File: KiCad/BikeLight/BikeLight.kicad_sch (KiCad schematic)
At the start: 19 parts, among them J1 Conn-01x02_P2.5mm_S2B-XH-A-BK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, J3 Conn-01x02_P2.5mm_S2B-XH-A-BK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, SW1 CK_KMS2xxG, U1 HT-CT62, U2 MPU-6050, U3 MCP1826S-33, U4 MAX17048, U5 TP4056-42-ESOP8, U6 MT3608

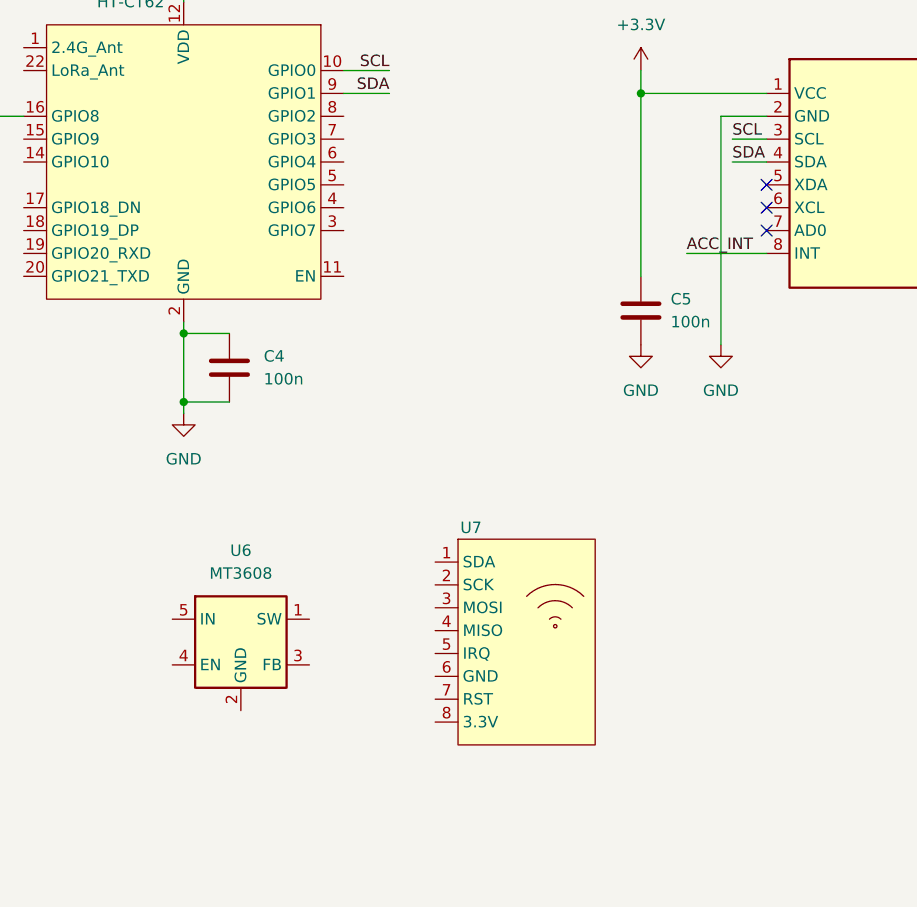
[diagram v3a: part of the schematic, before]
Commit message: Small adjustments to the RFID
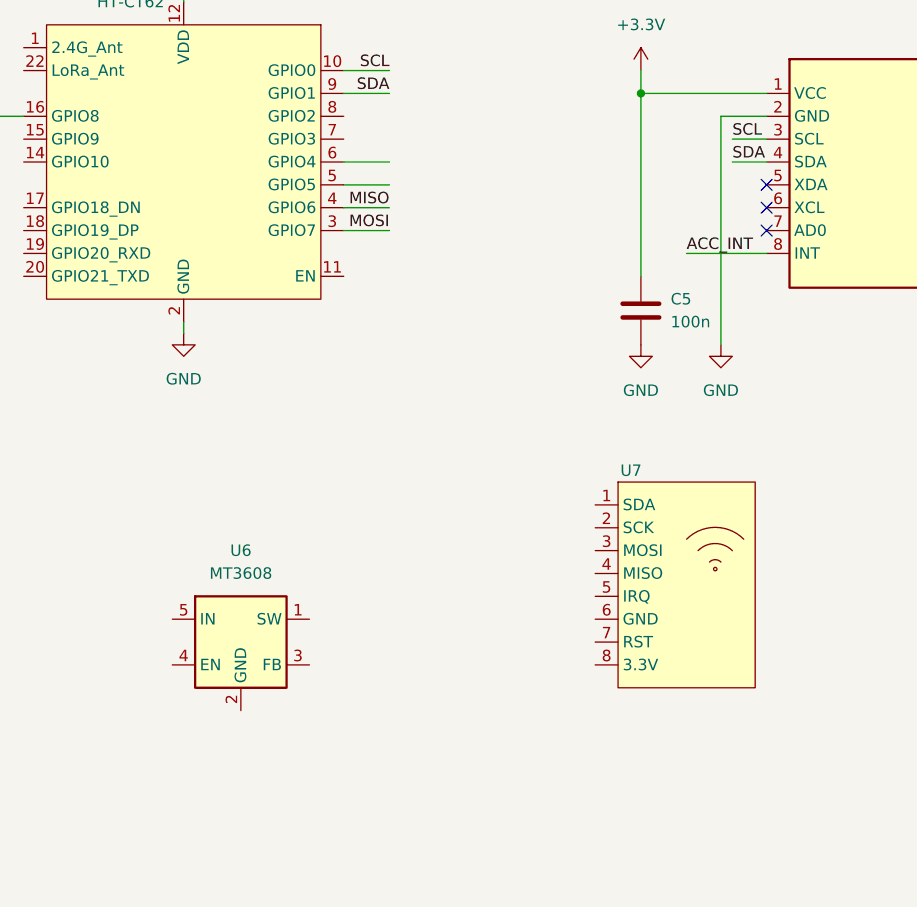
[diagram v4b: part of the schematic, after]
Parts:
- removed C4: 100n_0603_TCC0603X7R104K500CT, Capacitor_SMD:C_0603_1608Metric, symbol 00-kiml-capacitors-smd:100n_0603_TCC0603X7R104K500CT
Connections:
- net MOSI: now reaches U1.3 (GPIO7)
- net MISO: now reaches U1.4 (GPIO6)
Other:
- moved on the sheet: U7
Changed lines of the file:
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@@
 	)
 	(junction
-		(at 154.94 105.41)
-		(diameter 0)
-		(color 0 0 0 0)
-	)
-	(junction
 		(at 115.57 73.66)
 		(diameter 0)
@@
 	)
 	(junction
-		(at 154.94 97.79)
-		(diameter 0)
-		(color 0 0 0 0)
-	)
-	(junction
 		(at 128.27 121.92)
 		(diameter 0)
@@
 	(wire
 		(pts
-			(xy 63.5 97.79) (xy 63.5 99.06)
+			(xy 172.72 83.82) (xy 177.8 83.82)
 		)
 		(stroke
@@
 	(wire
 		(pts
-			(xy 91.44 73.66) (xy 100.33 73.66)
+			(xy 63.5 97.79) (xy 63.5 99.06)
 		)
 		(stroke
@@
 	(wire
 		(pts
-			(xy 80.01 157.48) (xy 95.25 157.48)
+			(xy 91.44 73.66) (xy 100.33 73.66)
 		)
 		(stroke
@@
 	(wire
 		(pts
-			(xy 100.33 73.66) (xy 102.87 73.66)
+			(xy 80.01 157.48) (xy 95.25 157.48)
 		)
 		(stroke
@@
 	(wire
 		(pts
-			(xy 113.03 154.94) (xy 118.11 154.94)
+			(xy 100.33 73.66) (xy 102.87 73.66)
 		)
 		(stroke
@@
 	(wire
 		(pts
-			(xy 154.94 97.79) (xy 160.02 97.79)
+			(xy 113.03 154.94) (xy 118.11 154.94)
 		)
 		(stroke
@@
 	(wire
 		(pts
-			(xy 205.74 71.12) (xy 219.71 71.12)
+			(xy 172.72 86.36) (xy 177.8 86.36)
 		)
 		(stroke
@@
 	(wire
 		(pts
-			(xy 154.94 105.41) (xy 154.94 97.79)
+			(xy 205.74 71.12) (xy 219.71 71.12)
 		)
 		(stroke
@@
 	(wire
 		(pts
-			(xy 214.63 73.66) (xy 214.63 99.06)
+			(xy 154.94 96.52) (xy 154.94 97.79)
 		)
 		(stroke
@@
 	(wire
 		(pts
-			(xy 154.94 44.45) (xy 162.56 44.45)
+			(xy 214.63 73.66) (xy 214.63 99.06)
 		)
 		(stroke
@@
 	(wire
 		(pts
-			(xy 90.17 154.94) (xy 90.17 167.64)
+			(xy 154.94 44.45) (xy 162.56 44.45)
 		)
 		(stroke
@@
 	(wire
 		(pts
-			(xy 115.57 73.66) (xy 113.03 73.66)
+			(xy 172.72 78.74) (xy 177.8 78.74)
 		)
 		(stroke
@@
 	(wire
 		(pts
-			(xy 80.01 157.48) (xy 80.01 160.02)
+			(xy 90.17 154.94) (xy 90.17 167.64)
 		)
 		(stroke
@@
 	(wire
 		(pts
-			(xy 215.9 76.2) (xy 219.71 76.2)
+			(xy 115.57 73.66) (xy 113.03 73.66)
 		)
 		(stroke
@@
 	(wire
 		(pts
-			(xy 114.3 129.54) (xy 114.3 132.08)
+			(xy 80.01 157.48) (xy 80.01 160.02)
 		)
 		(stroke
@@
 	(wire
 		(pts
-			(xy 154.94 105.41) (xy 160.02 105.41)
+			(xy 215.9 76.2) (xy 219.71 76.2)
 		)
 		(stroke
@@
 	(wire
 		(pts
-			(xy 80.01 160.02) (xy 95.25 160.02)
+			(xy 114.3 129.54) (xy 114.3 132.08)
 		)
 		(stroke
@@
 	(wire
 		(pts
-			(xy 115.57 88.9) (xy 115.57 73.66)
+			(xy 80.01 160.02) (xy 95.25 160.02)
 		)
 		(stroke
@@
 	(wire
 		(pts
-			(xy 80.01 152.4) (xy 80.01 157.48)
+			(xy 115.57 88.9) (xy 115.57 73.66)
 		)
 		(stroke
@@
 	(wire
 		(pts
-			(xy 154.94 97.79) (xy 154.94 96.52)
+			(xy 80.01 152.4) (xy 80.01 157.48)
 		)
 		(stroke
@@
 	(wire
 		(pts
-			(xy 113.03 160.02) (xy 118.11 160.02)
+			(xy 172.72 81.28) (xy 177.8 81.28)
 		)
 		(stroke
@@
 	(wire
 		(pts
-			(xy 128.27 119.38) (xy 128.27 121.92)
+			(xy 113.03 160.02) (xy 118.11 160.02)
 		)
 		(stroke
@@
 	(wire
 		(pts
-			(xy 95.25 162.56) (xy 95.25 167.64)
+			(xy 128.27 119.38) (xy 128.27 121.92)
 		)
 		(stroke
@@
 	(wire
 		(pts
-			(xy 215.9 78.74) (xy 219.71 78.74)
+			(xy 95.25 162.56) (xy 95.25 167.64)
 		)
 		(stroke
@@
 	(wire
 		(pts
-			(xy 95.25 154.94) (xy 90.17 154.94)
+			(xy 215.9 78.74) (xy 219.71 78.74)
 		)
 		(stroke
@@
 	(wire
 		(pts
-			(xy 154.94 106.68) (xy 154.94 105.41)
+			(xy 95.25 154.94) (xy 90.17 154.94)
 		)
 		(stroke
@@
 			"AAAAAADw5If81AEAAODkh/zUAQAAsEHO/NQBAAAAAAAAAAAAAPDkh/zUAQAA4OSH/NQBAADQQc78"
 			"1AEAAAAAAAAAAAAAIAAAAG0CAAAAAAAAAAAAACgcAAAAAAAAAAABAAAAAABA98n81AEAAKoCAAAA"
-			"AAAAIK2q/NQBAAD/////AAD//wAAAAABAAAAAAAAAAAAAAAAAAAAAAAAAAAAAAAAAA=="
+			"AAAAIK2q/NQBAAD/////AAD//wAAAAABAAAAAAAAAAAAAAAAAAAAAAAAAAAAAAAAAAAAAAAAAAAA"
+			"AAAAAAAAAAAAAAAAAAAAAAAAAAAAAAAAAAAAAAAAAAAAAAAAAAAAAAAAAAAAAAAAAAAAAAAAAAAA"
+			"AAAAAAAAAAAAAAAAAAAAAAAAAAAAAAAAAAAAAAAAAAAAAAAAAAAAAAAAAAAAAAAAAAAAAAAAAAAA"
+			"AAAAAAAAAAAAAAAAAAAAAAAAAAAAAAAAAAAAAAAAAAAAAAAAAAAAAAAAAAAAAAAAAAAAAAAAAAAA"
+			"AAAAAAAAAAAAAAAAAAAAAAAAAAAAAAAAAAAAAAAAAAAAAAAAAAAAAAAAAAAAAAAAAAAAAAAAAAAA"
+			"AAAAAAAAAAAAAAAAAAAAAAAAAAAAAAAAAAAAAAAAAAAAAAAAAAAAAAAAAAAAAAAAAAAAAAAAAAAA"
+			"AAAAAAAAAAAAAAAAAAAAAAAAAAAAAAAAAAAAAAAAAAAAAAAAAAAAAAAAAAAAAAAAAAAAAAAAAAAA"
+			"AAAAAAAAAAAAAAAAAAAAAAAAAAAAAAAAAAAAAAAAAAAAAAAAAAAAAAAAAAAAAAAAAAAAAAAAAAAA"
+			"AAAAAAAAAAAAAAAAAAAAAAAAAAAAAAAAAAAAAAAAAAAAAAAAAAAAAAAAAAAAAAAAAAAAAAAAAAAA"
+			"AAAAAAAAAAAAAAAAAAAAAAAAAAAAAAAAAAAAAAAAAAAAAAAAAAAAAAAAAAAAAAAAAAAAAAAAAAAA"
+			"AAAAAAAAAAAAAAAAAAAAAAAAAAAAAAAAAAAAAAAAAAAAAAAAAAAAAAAAAAAAAAAAAAAAAAAAAAAA"
+			"AAAAAAAAAAAAAAAAAAAAAAAAAAAAAAAAAAAAAAAAAAAAAAAAAAAAAAAAAAAAAAAAAAAAAAAAAAAA"
+			"AAAAAAAAAAAAAAAAAAAAAAAAAAAAAAAAAAAAAAAAAAAAAAAAAAAAAAAAAAAAAAAAAAAAAAAAAAAA"
+			"AAAAAAAAAAAAAAAAAAAAAAAAAAAAAAAAAAAAAAAAAAAAAAAAAAAAAAAAAAAAAAAAAAAAAAAAAAAA"
+			"AAAAAAAAAAAAAAAAAAAAAAAAAAAAAAAAAAAAAAAAAAAAAAAAAAAAAAAAAAAAAAAAAAAAAAAAAAAA"
+			"AAAAAAAAAAAAAAAAAAAAAAAAAAAAAAAAAAAAAAAAAAAAAAAAAAAAAAAAAAAAAAAAAAAAAAAAAAAA"
+			"AAAAAAAAAAAAAAAAAAAAAAAAAAAAAAAAAAAAAAAAAAAAAAAAAAAAAAAAAAAAAAAAAAAAAAAAAAAA"
+			"AAAAAAAAAAAAAAAAAAAAAAAAAAAAAAAAAAAAAAAAAAAAAAAAAAAAAAAAAAAAAAAAAAAAAAAAAAAA"
+			"AAAAAAAAAAAAAAAAAAAAAAAAAAAAAAAAAAAAAAAAAAAAAAAAAAAAAAAAAAAAAAAAAA=="
+		)
+	)
+	(label "MOSI"
+		(at 177.8 86.36 180)
+		(effects
+			(font
+				(size 1.27 1.27)
+			)
+			(justify right bottom)
 		)
 	)
@@
 		)
 	)
+	(label "MISO"
+		(at 177.8 83.82 180)
+		(effects
+			(font
+				(size 1.27 1.27)
+			)
+			(justify right bottom)
+		)
+	)
 	(label "SDA"
 		(at 118.11 162.56 180)
@@
 	(symbol
 		(lib_id "power:GND")
-		(at 154.94 106.68 0)
+		(at 154.94 97.79 0)
 		(unit 1)
 		(exclude_from_sim no)
@@
 		(fields_autoplaced yes)
 		(property "Reference" "#PWR03"
-			(at 154.94 113.03 0)
+			(at 154.94 104.14 0)
 			(effects
 				(font
@@
 		)
 		(property "Value" "GND"
-			(at 154.94 111.76 0)
+			(at 154.94 102.87 0)
 			(effects
 				(font
@@
 		)
 		(property "Footprint" ""
-			(at 154.94 106.68 0)
+			(at 154.94 97.79 0)
 			(effects
 				(font
@@
 		)
 		(property "Datasheet" ""
-			(at 154.94 106.68 0)
+			(at 154.94 97.79 0)
 			(effects
 				(font
@@
 		)
 		(property "Description" "Power symbol creates a global label with name \"GND\" , ground"
-			(at 154.94 106.68 0)
+			(at 154.94 97.79 0)
 			(effects
 				(font
@@
 	(symbol
 		(lib_id "Personal_Library:RFID-RC522")
-		(at 185.42 118.11 0)
+		(at 203.2 111.76 0)
 		(unit 1)
 		(exclude_from_sim no)
@@
 		(dnp no)
 		(property "Reference" "U7"
-			(at 185.674 119.38 0)
+			(at 203.454 113.03 0)
 			(effects
 				(font
@@
 		)
 		(property "Value" "~"
-			(at 201.93 133.35 0)
+			(at 219.71 127 0)
 			(effects
 				(font
@@
 		)
 		(property "Footprint" ""
-			(at 185.42 118.11 0)
+			(at 203.2 111.76 0)
 			(effects
 				(font
@@
 		)
 		(property "Datasheet" ""
-			(at 185.42 118.11 0)
+			(at 203.2 111.76 0)
 			(effects
 				(font
@@
 		)
 		(property "Description" ""
-			(at 185.42 118.11 0)
+			(at 203.2 111.76 0)
 			(effects
 				(font
@@
 					(unit 1)
 				)
-			)
-		)
-	)
-	(symbol
-		(lib_id "00-kiml-capacitors-smd:100n_0603_TCC0603X7R104K500CT")
-		(at 160.02 101.6 0)
-		(unit 1)
-		(exclude_from_sim no)
-		(in_bom yes)
-		(on_board yes)
-		(dnp no)
-		(fields_autoplaced yes)
-		(property "Reference" "C4"
-			(at 163.83 100.3299 0)
-			(effects
-				(font
-					(size 1.27 1.27)
-				)
-				(justify left)
-			)
-		)
-		(property "Value" "100n_0603_TCC0603X7R104K500CT"
-			(at 144.78 69.85 0)
-			(effects
-				(font
-					(size 1.27 1.27)
-				)
-				(justify left)
-				(hide yes)
-			)
-		)
-		(property "Footprint" "Capacitor_SMD:C_0603_1608Metric"
-			(at 160.02 85.09 0)
-			(effects
-				(font
-					(size 1.27 1.27)
-				)
-				(hide yes)
-			)
-		)
-		(property "Datasheet" "https://datasheet.lcsc.com/lcsc/1810181652_CCTC-TCC0603X7R104K500CT_C282519.pdf"
-			(at 160.02 80.01 0)
-			(effects
-				(font
-					(size 1.27 1.27)
-				)
-				(hide yes)
-			)
-		)
-		(property "Description" "50V 100nF X7R ±10% 0603 Multilayer Ceramic Capacitors MLCC"
-			(at 160.02 101.6 0)
-			(effects
-				(font
-					(size 1.27 1.27)
-				)
-				(hide yes)
-			)
-		)
-		(property "UserValue" "100n"
-			(at 163.83 102.8699 0)
-			(effects
-				(font
-					(size 1.27 1.27)
-				)
-				(justify left)
-			)
-		)
-		(property "MFR" "CCTC"
-			(at 160.02 82.55 0)
-			(effects
-				(font
-					(size 1.27 1.27)
-				)
-				(hide yes)
-			)
-		)
-		(property "MPN" "TCC0603X7R104K500CT"
-			(at 160.02 77.47 0)
-			(effects
-				(font
-					(size 1.27 1.27)
-				)
-				(hide yes)
-			)
-		)
-		(property "SPL1" "LCSC"
-			(at 160.02 121.92 0)
-			(effects
-				(font
-					(size 1.27 1.27)
-				)
-				(hide yes)
-			)
-		)
-		(property "SPN1" "C307331"
-			(at 160.02 125.095 0)
-			(effects
-				(font
-					(size 1.27 1.27)
-				)
-				(hide yes)
-			)
-		)
-		(property "LNK1" "https://www.lcsc.com/product-detail/Multilayer-Ceramic-Capacitors-MLCC-SMD-SMT_CCTC-TCC0603X7R104K500CT_C282519.html"
-			(at 159.385 118.745 0)
-			(effects
-				(font
-					(size 1.27 1.27)
-				)
-				(hide yes)
-			)
-		)
-		(property "Tolerance" "10%"
-			(at 160.02 72.39 0)
-			(effects
-				(font
-					(size 1.27 1.27)
-				)
-				(hide yes)
-			)
-		)
-		(property "Rating" "50V"
-			(at 160.02 74.93 0)
-			(effects
-				(font
-					(size 1.27 1.27)
-				)
-				(hide yes)
-			)
-		)
-		(pin "1"
-		)
-		(pin "2"
-		)
-		(instances
-			(project ""
-				(path "/bc4a3ac7-23ef-4452-9888-c2aa5f8e2382"
-					(reference "C4")
-					(unit 1)
-				)

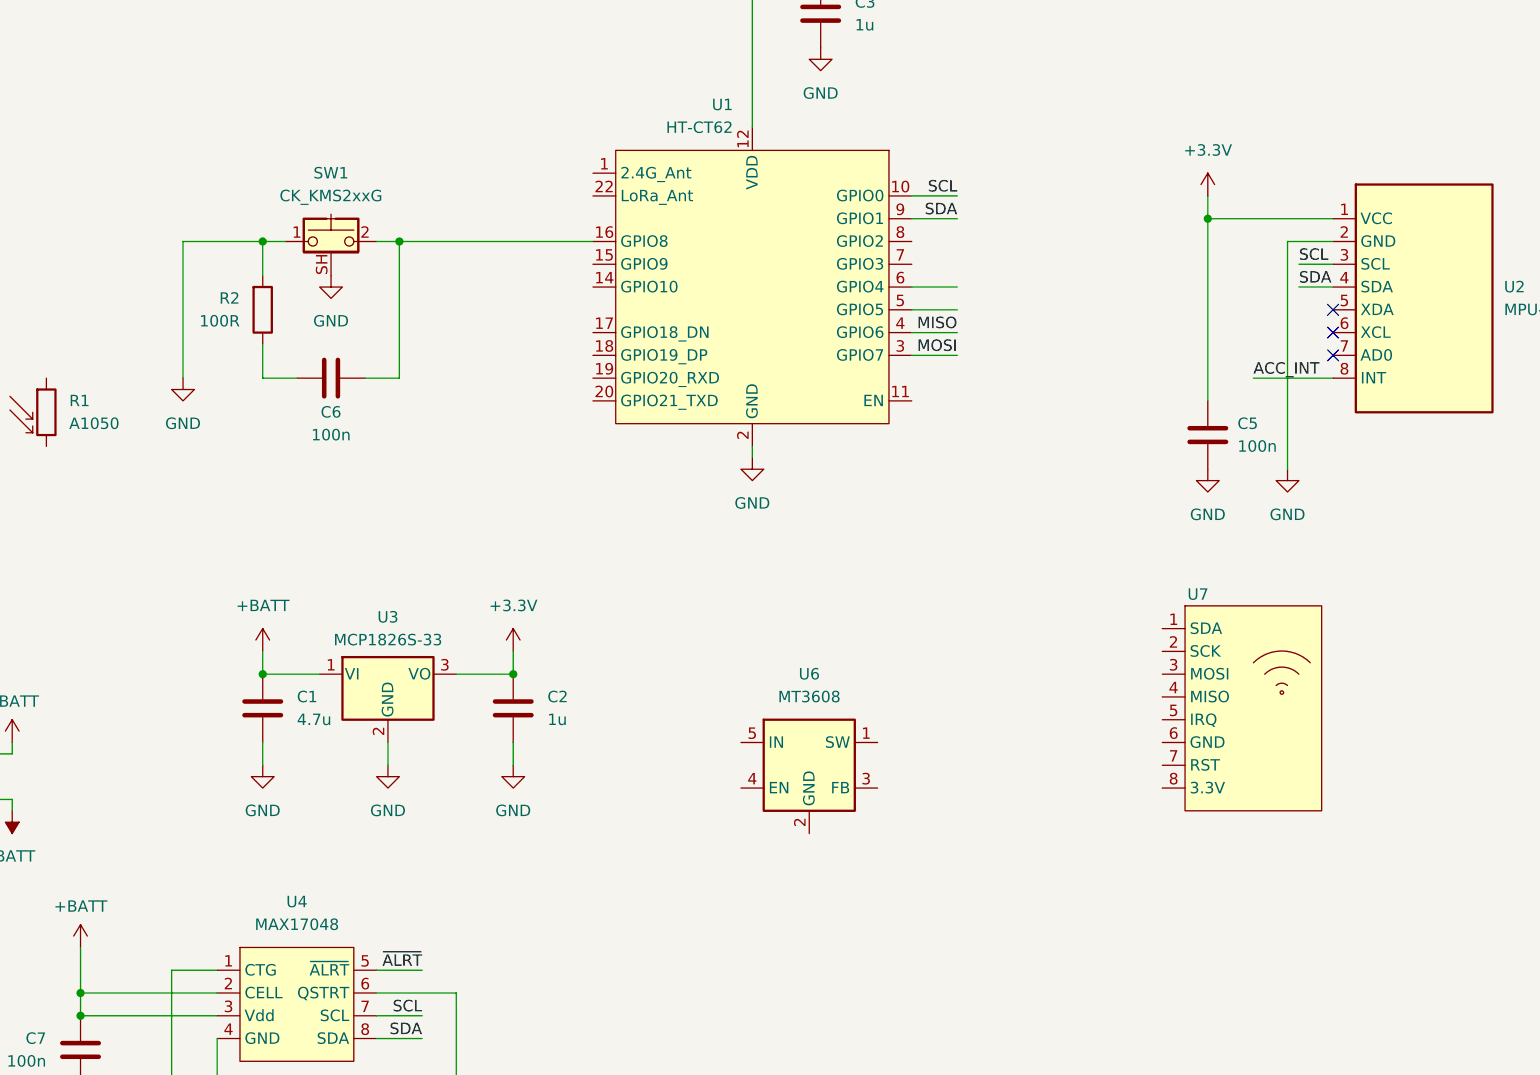
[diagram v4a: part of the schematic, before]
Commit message: Changed RFID to use I2C
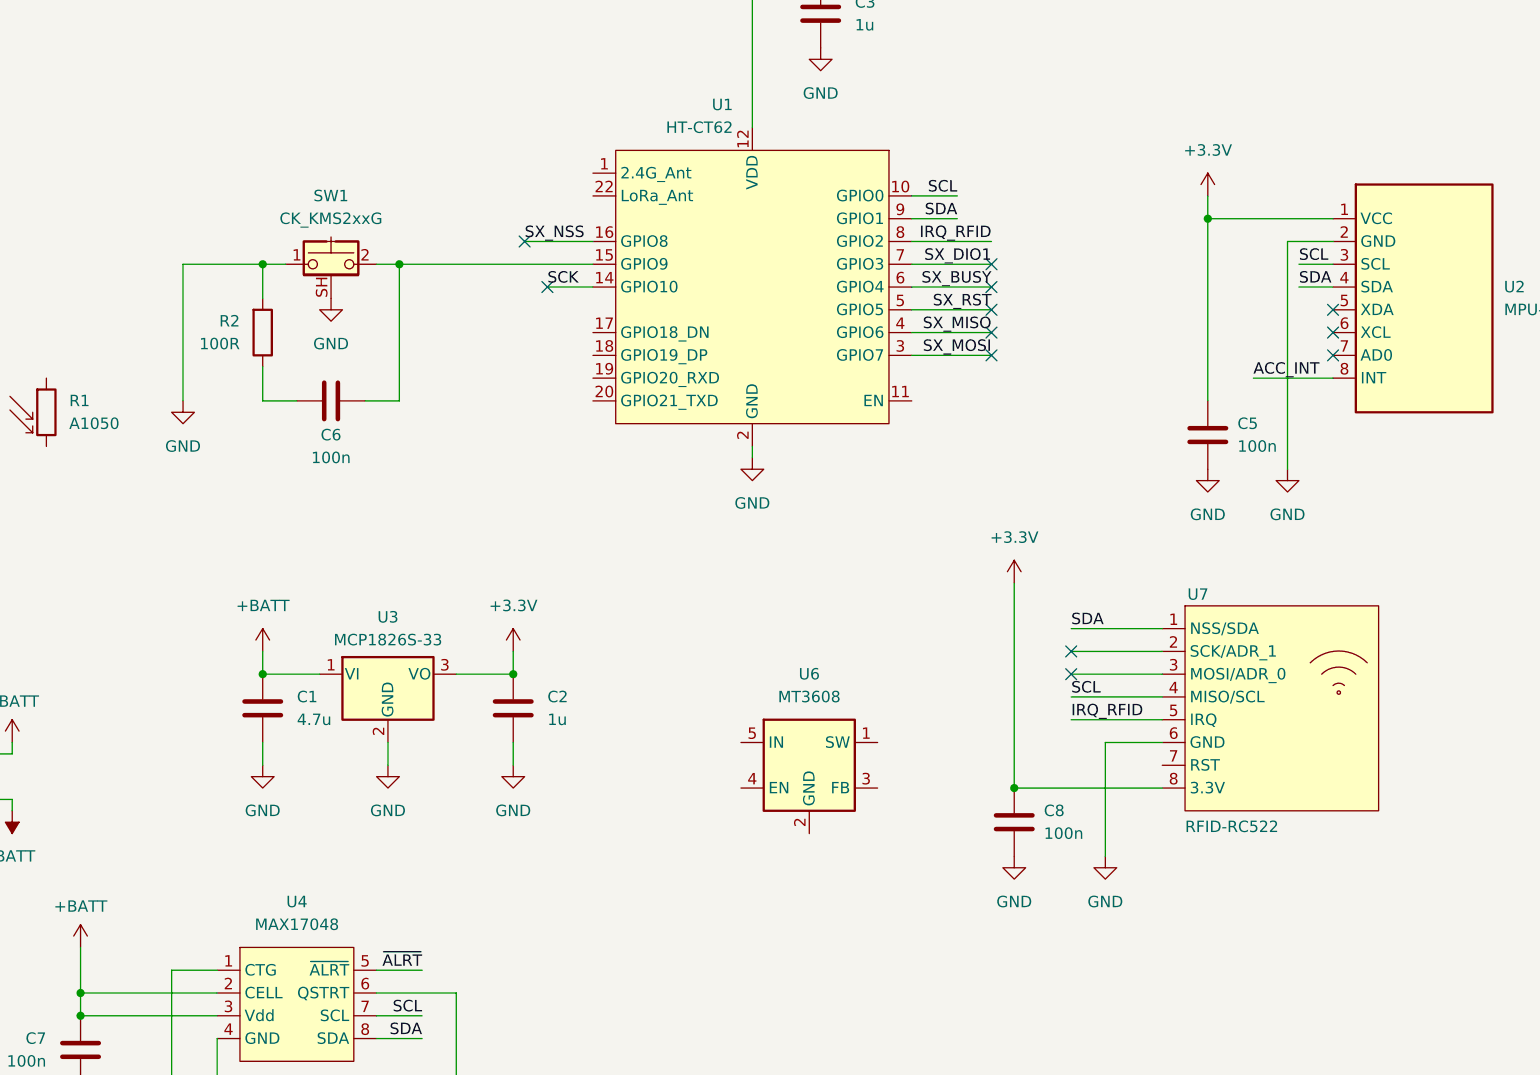
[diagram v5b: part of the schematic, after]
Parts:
- added C8: 100n_0603_TCC0603X7R104K500CT, Capacitor_SMD:C_0603_1608Metric, symbol 00-kiml-capacitors-smd:100n_0603_TCC0603X7R104K500CT
- U7: value ~ -> RFID-RC522
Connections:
- net +3.3V: now also U7.8 (3.3V), C8.1
- net GND: now also U7.6 (GND), C8.2
- net SCL: now also U7.4 (MISO/SCL)
- net SDA: now also U7.1 (NSS/SDA)
- net at C6.2, SW1.2: now also U1.15 (GPIO9); no longer U1.16 (GPIO8)
- net IRQ_RFID: now reaches U7.5 (IRQ)
- net IRQ_RFID: now also U1.8 (GPIO2)
- net SCK: now reaches U1.14 (GPIO10)
- net SX_RST: now reaches U1.5 (GPIO5)
- net SX_BUSY: now reaches U1.6 (GPIO4)
- net SX_DIO1: now reaches U1.7 (GPIO3)
- net MISO renamed SX_MISO
- net MOSI renamed SX_MOSI
- new net SX_NSS: U1.16 (GPIO8)
- no-connect marks 3 -> 12
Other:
- moved on the sheet: C6, R2, SW1, U7
